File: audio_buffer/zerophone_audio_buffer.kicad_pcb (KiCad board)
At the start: 2 copper layers, 13.2 x 10.7 mm, 7 parts, among them P1 INPUT_CONN, P2 OUTPUT_CONN, U1 LM1117-2.5, U2 NC7WZ16

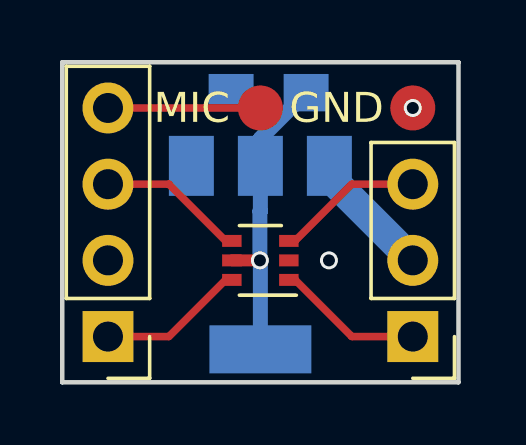
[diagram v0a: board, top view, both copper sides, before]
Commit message: Updated audio buffer board
-Changed power regulator to a low-noise one
-Moved GND testpoint so that adding a connector is  theoretically
possible, just in case
-Added auxiliary axis
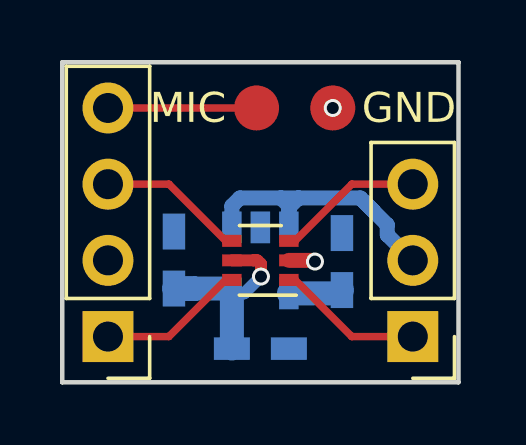
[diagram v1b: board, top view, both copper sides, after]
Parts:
- added C2: 470pF, Capacitors_SMD:C_0603_HandSoldering, B.Cu at (134.8, 99.1)
- added C3: 2.2uF, Capacitors_SMD:C_0603_HandSoldering, B.Cu at (132.1, 102.0)
- C1: value C_Small -> 100nF; footprint Capacitors_SMD:C_0805_HandSoldering -> Capacitors_SMD:C_0603_HandSoldering
- U1: value LM1117-2.5 -> MIC5219-3.3BM5; footprint TO_SOT_Packages_SMD:SOT-223 -> TO_SOT_Packages_SMD:SOT-23-5
- moved C1 6.41 mm to (129.2, 99.0), turned to 90 degrees
- moved W2 2.67 mm to (134.5, 94.0)
- moved W1 0.13 mm to (132.0, 94.0)
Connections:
- C1 pad 1: +2V5 -> +3V3
- P1 pad 2: +3V3 -> VCC
- U1 pad 1: GND -> VCC
- U1 pad 2: +2V5 -> GND
- U1 pad 3: +3V3 -> VCC
- U1 pad 4: +2V5 -> Net-(C2-Pad1)
- U2 pad 5: +2V5 -> +3V3
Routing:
- net VCC: track 0.00 -> 10.8 mm
- net +2V5: track 10.4 -> 0.00 mm, vias 1 -> 0
- net +3V3: track 4.30 -> 7.05 mm, vias 0 -> 1
- net Net-(C2-Pad1): track 0.00 -> 1.82 mm
- net GND: track 0.00 -> 0.89 mm, vias 1 -> 2
- net (no net): vias 1 -> 0
